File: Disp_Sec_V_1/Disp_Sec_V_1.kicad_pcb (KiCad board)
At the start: 2 copper layers, 146 x 62 mm, 57 parts, among them J1 DC Supply, J2 Contacto A (N.O), J3 Contacto F (N.0), K1 FINDER-36.11, K2 FINDER-36.11, K3 FINDER-36.11, Q1 BC337, Q2 BC337, Q3 BC337, Q4 BC337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

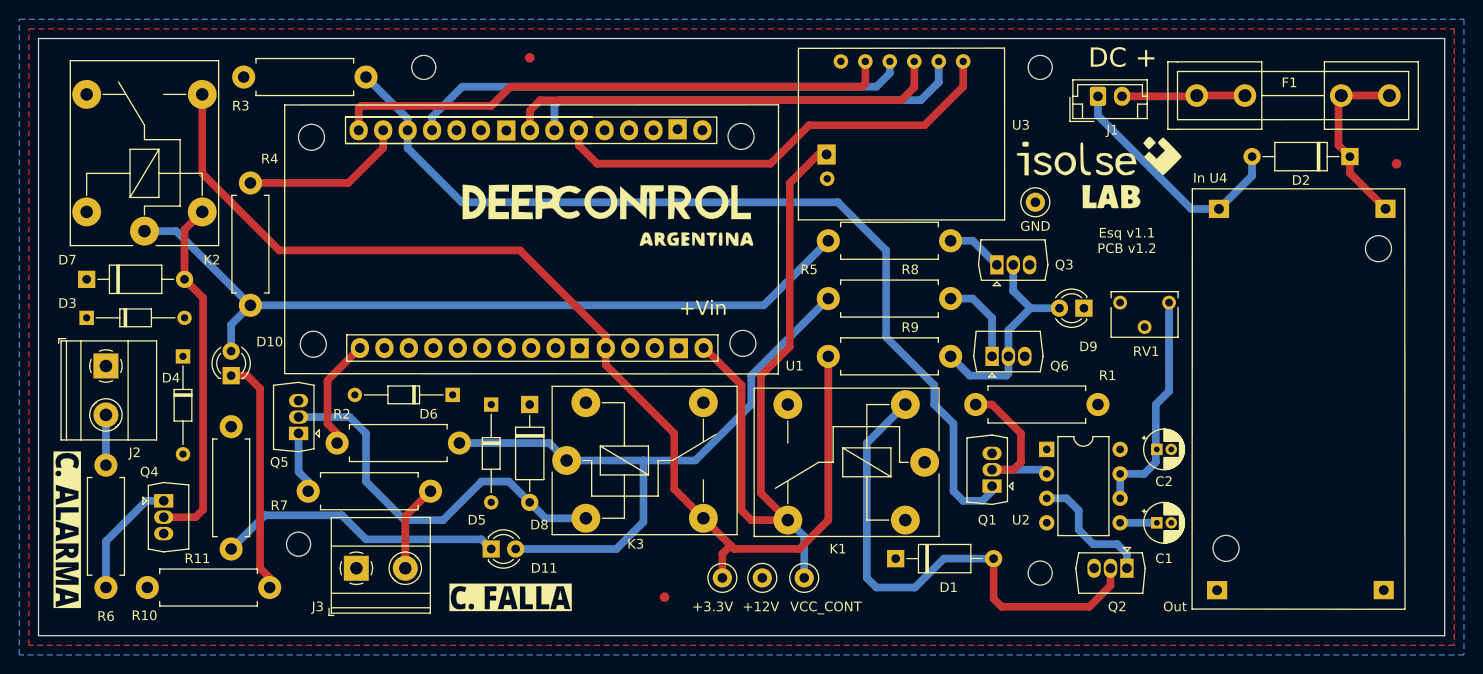
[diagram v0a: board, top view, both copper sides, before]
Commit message: Correcion: Vias/Soldadura Back
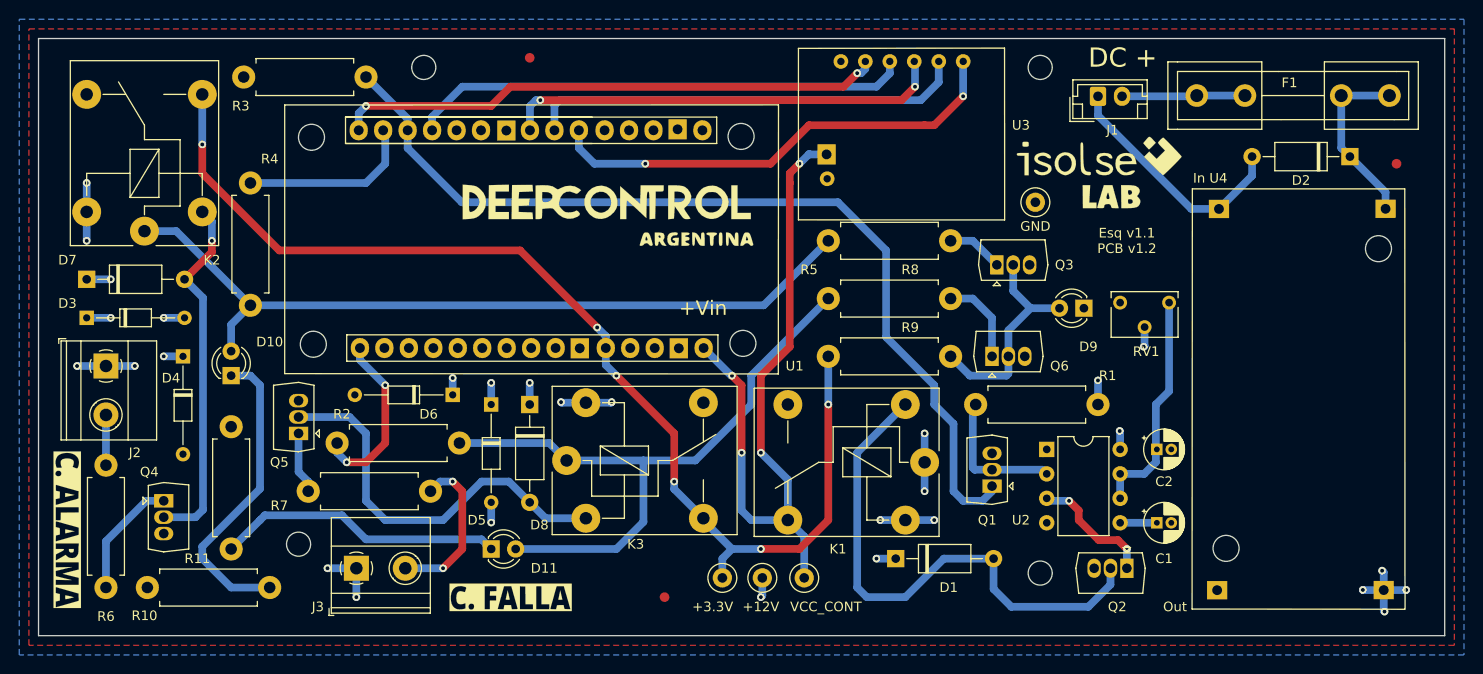
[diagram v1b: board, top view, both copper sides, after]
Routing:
- net +12V: track 1.00 -> 72.8 mm, vias 0 -> 29
- net Net-(J3-Pad2): track 9.09 -> 16.9 mm, vias 0 -> 2
- net Net-(D10-Pad1): track 24.6 -> 32.1 mm
- net Net-(R2-Pad1): track 11.7 -> 18.2 mm, vias 0 -> 2
- net Net-(Q1-Pad2): track 18.1 -> 14.6 mm
- net Net-(D1-Pad2): track 53.8 -> 56.0 mm
- net /ALARM_PIN: track 17.1 -> 18.4 mm
- net Net-(D8-Pad2): track 40.4 -> 41.6 mm
- net /CE: track 58.2 -> 57.1 mm, vias 0 -> 2
- net Net-(D7-Pad2): track 36.9 -> 37.7 mm, vias 0 -> 1
- net /MISO: track 48.2 -> 48.9 mm, vias 0 -> 2
- net /VCC_CONT: track 72.9 -> 73.6 mm, vias 0 -> 4
- net Net-(F1-Pad2): track 12.5 -> 13.0 mm
- net /SCK: track 45.6 -> 46.0 mm, vias 0 -> 2
- net Net-(Q2-Pad1): track 13.4 -> 13.1 mm, vias 0 -> 2
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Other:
- rule pad_to_mask_clearance: 0.05 -> 0
